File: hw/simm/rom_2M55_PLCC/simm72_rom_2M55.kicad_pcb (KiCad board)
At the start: 4 copper layers, 108 x 19.1 mm, 9 parts, among them J1 SIMM72, U1 SST39SF040, U2 SST39SF040, U3 SST39SF040, U4 SST39SF040

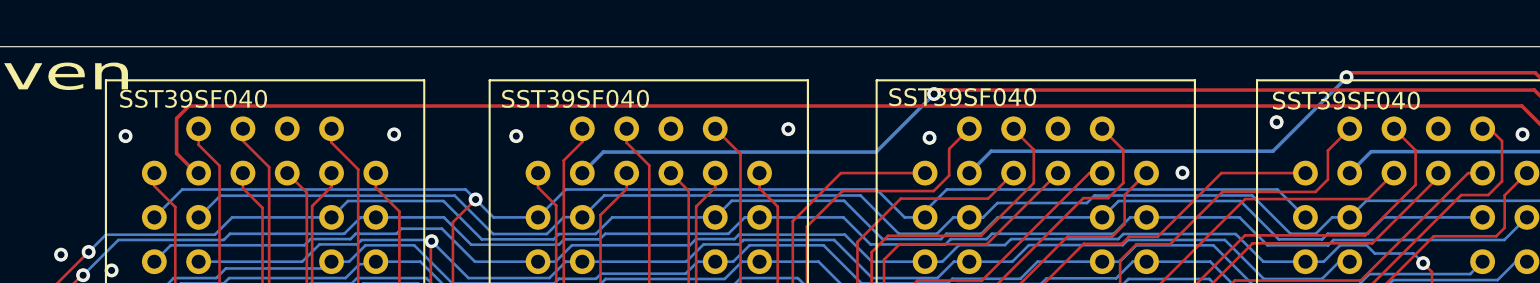
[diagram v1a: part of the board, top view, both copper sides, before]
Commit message: Update PLCC rom preview image
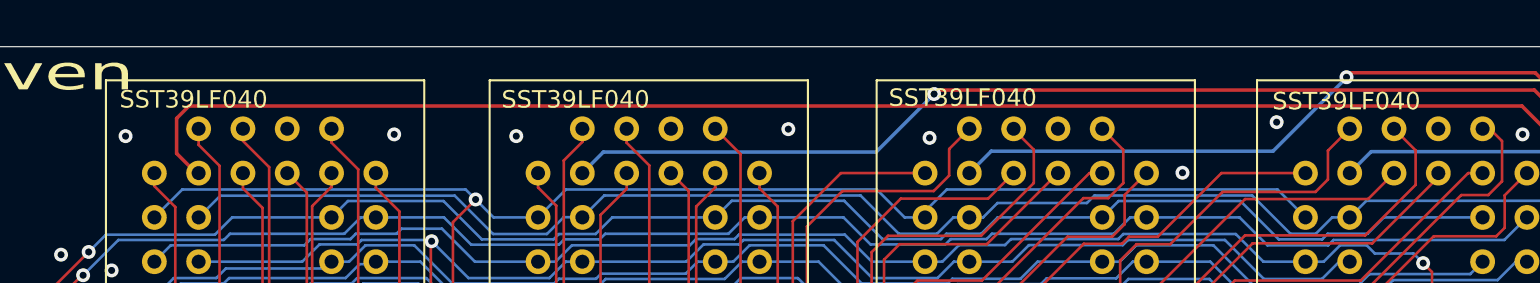
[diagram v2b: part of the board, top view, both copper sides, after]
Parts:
- U1, U2, U3, U4: value SST39SF040 -> SST39LF040
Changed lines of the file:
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@@
         (effects (font (size 1 1) (thickness 0.15)))
     )
-    (fp_text value "SST39SF040" (at 2.93 14.38) (layer "F.SilkS")
+    (fp_text value "SST39LF040" (at 2.93 14.38) (layer "F.SilkS")
         (effects (font (size 1 1) (thickness 0.15)))
     )
@@
         (effects (font (size 1 1) (thickness 0.15)))
     )
-    (fp_text value "SST39SF040" (at 2.73 14.28) (layer "F.SilkS")
+    (fp_text value "SST39LF040" (at 2.73 14.28) (layer "F.SilkS")
         (effects (font (size 1 1) (thickness 0.15)))
     )
@@
         (effects (font (size 1 1) (thickness 0.15)))
     )
-    (fp_text value "SST39SF040" (at 2.83 14.38) (layer "F.SilkS")
+    (fp_text value "SST39LF040" (at 2.83 14.38) (layer "F.SilkS")
         (effects (font (size 1 1) (thickness 0.15)))
     )
@@
         (effects (font (size 1 1) (thickness 0.15)))
     )
-    (fp_text value "SST39SF040" (at 2.92 14.48) (layer "F.SilkS")
-        (effects (font (size 1 1) (thickness 0.15)))
-    )
+    (fp_text value "SST39LF040" (at 2.92 14.48) (layer "F.SilkS")
+        (effects (font (size 1 1) (thickness 0.15)))
+    )
